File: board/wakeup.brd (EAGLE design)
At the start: 65 x 56 mm, 23 parts, among them IC2 ATMEGA48/88/168-AU, K1 PIN20X2, U1 EEPROM24

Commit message: Added gerber file
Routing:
- net GND: track 113.3 -> 104.1 mm, vias 6 -> 10
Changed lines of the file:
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@@
 <contactref element="CREE_LED1" pad="5"/>
 <contactref element="CREE_LED1" pad="7"/>
-<wire x1="28.4083875" y1="43.246209375" x2="28.4083875" y2="37.5916125" width="0.6096" layer="1"/>
-<wire x1="28.4083875" y1="37.5916125" x2="32" y2="34" width="0.6096" layer="1"/>
-<wire x1="32" y1="34" x2="32" y2="31.33" width="0.6096" layer="1"/>
 <wire x1="32" y1="31.33" x2="31.67" y2="31" width="0.6096" layer="1"/>
 <via x="37" y="36" extent="1-16" drill="0.6" shape="square"/>
@@
 <wire x1="51.44011875" y1="35.60608125" x2="51.44011875" y2="39.55988125" width="0.4064" layer="1"/>
 <wire x1="51.44011875" y1="39.55988125" x2="51" y2="40" width="0.4064" layer="1"/>
-<wire x1="61.865" y1="36.625" x2="61.865" y2="37.895" width="0" layer="19" extent="1-1"/>
-<wire x1="61.865" y1="35.355" x2="61.865" y2="36.625" width="0" layer="19" extent="1-1"/>
-<wire x1="61.865" y1="39.165" x2="61.865" y2="37.895" width="0" layer="19" extent="1-1"/>
-<wire x1="41.7074" y1="36.2" x2="42.709359375" y2="36.1917" width="0" layer="19" extent="1-1"/>
-<wire x1="20.003" y1="31" x2="22.67" y2="31" width="0" layer="19" extent="1-1"/>
-<wire x1="20.003" y1="26" x2="22.67" y2="26" width="0" layer="19" extent="1-1"/>
-<wire x1="20.003" y1="21" x2="22.67" y2="21" width="0" layer="19" extent="1-1"/>
-<wire x1="29.003" y1="16" x2="31.67" y2="16" width="0" layer="19" extent="1-1"/>
-<wire x1="22.67" y1="16" x2="22" y2="16" width="0" layer="19" extent="1-1"/>
-<wire x1="20.003" y1="16" x2="22" y2="16" width="0" layer="19" extent="1-1"/>
-<wire x1="32" y1="31.33" x2="35" y2="31" width="0" layer="19" extent="1-1"/>
-<wire x1="24" y1="42" x2="24" y2="43" width="0" layer="19" extent="1-1"/>
-<wire x1="24" y1="41" x2="24.2512625" y2="41.7487375" width="0" layer="19" extent="1-1"/>
-<wire x1="24.260740625" y1="40.260740625" x2="24" y2="41" width="0" layer="19" extent="1-1"/>
-<wire x1="24" y1="39" x2="24" y2="40" width="0" layer="19" extent="1-1"/>
-<wire x1="29.003" y1="31" x2="31.67" y2="31" width="0" layer="19" extent="1-1"/>
-<wire x1="31.67" y1="26" x2="35" y2="26" width="0" layer="19" extent="1-1"/>
-<wire x1="29.003" y1="26" x2="31.67" y2="26" width="0" layer="19" extent="1-1"/>
-<wire x1="31.67" y1="21" x2="35" y2="21" width="0" layer="19" extent="1-1"/>
-<wire x1="29.003" y1="21" x2="31.67" y2="21" width="0" layer="19" extent="1-1"/>
+<wire x1="28.4083875" y1="39" x2="28.4083875" y2="43.246209375" width="0.4064" layer="1"/>
+<via x="30.1" y="44" extent="1-16" drill="0.9" shape="square"/>
+<via x="30.1" y="42" extent="1-16" drill="0.9" shape="square"/>
+<via x="30.1" y="40" extent="1-16" drill="0.9" shape="square"/>
+<via x="30.1" y="38" extent="1-16" drill="0.9" shape="square"/>
+<polygon width="0.4064" layer="1">
+<vertex x="28" y="37"/>
+<vertex x="28" y="45"/>
+<vertex x="31" y="45"/>
+<vertex x="31" y="37"/>
+</polygon>
 </signal>
 <signal name="+3V3">
@@
 <signal name="N$1">
 </signal>
+<signal name="N$2">
+</signal>
 </signals>

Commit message: Added pin header for tm1637 7-Segment display
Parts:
- added SL3: (no value), con-amp-quick:04P
- moved SL2 7.07 mm to (45.0, 43.0)
- moved C2 1.41 mm to (39.0, 35.0), turned to 90 degrees
- moved C3 1.41 mm to (39.0, 39.0), turned to 270 degrees
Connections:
- net +5V: now also SL3.1
- net GND: now also SL3.4
- net MISO_SPI: now also SL3.2
- net SCLK_SPI: now also SL3.3
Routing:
- net +5V: track 44.0 -> 73.5 mm
- net SCLK_SPI: track 0.00 -> 9.04 mm
- net MISO_SPI: track 0.00 -> 9.04 mm
- net VCC: track 65.2 -> 59.5 mm
- net GND: track 104.1 -> 101.5 mm
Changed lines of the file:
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@@
 <attribute name="OC_NEWARK" value="unknown" x="12" y="28" size="1.778" layer="27" rot="R90" display="off"/>
 </element>
-<element name="SL2" library="con-amp-quick" package="02P" value="" x="38" y="44" rot="R180">
-<attribute name="MF" value="" x="38" y="44" size="1.778" layer="27" rot="R180" display="off"/>
-<attribute name="MPN" value="" x="38" y="44" size="1.778" layer="27" rot="R180" display="off"/>
-<attribute name="OC_FARNELL" value="unknown" x="38" y="44" size="1.778" layer="27" rot="R180" display="off"/>
-<attribute name="OC_NEWARK" value="unknown" x="38" y="44" size="1.778" layer="27" rot="R180" display="off"/>
+<element name="SL2" library="con-amp-quick" package="02P" value="" x="45" y="43" rot="R180">
+<attribute name="MF" value="" x="45" y="43" size="1.778" layer="27" rot="R180" display="off"/>
+<attribute name="MPN" value="" x="45" y="43" size="1.778" layer="27" rot="R180" display="off"/>
+<attribute name="OC_FARNELL" value="unknown" x="45" y="43" size="1.778" layer="27" rot="R180" display="off"/>
+<attribute name="OC_NEWARK" value="unknown" x="45" y="43" size="1.778" layer="27" rot="R180" display="off"/>
 </element>
-<element name="C2" library="rcl" package="C0805" value="47nF" x="38" y="34" rot="R180"/>
+<element name="C2" library="rcl" package="C0805" value="47nF" x="39" y="35" rot="R90"/>
 <element name="U$7" library="1" package="SOT" value="AMC7135" x="32" y="31" rot="R270"/>
 <element name="U$8" library="1" package="SOT" value="AMC7135" x="23" y="31" rot="R270"/>
@@
 <element name="U$6" library="1" package="SOT" value="AMC7135" x="32" y="16" rot="R270"/>
 <element name="IC2" library="atmega8" package="TQFP32-08" value="ATMEGA48/88/168-AU" x="46" y="35"/>
-<element name="C3" library="rcl" package="C0805" value="47nF" x="38" y="38" rot="R180"/>
+<element name="C3" library="rcl" package="C0805" value="47nF" x="39" y="39" rot="R270"/>
 <element name="J1" library="con-jack" package="SPC4078" value="" x="12" y="13" rot="R90">
 <attribute name="OC_FARNELL" value="unknown" x="12" y="13" size="1.778" layer="27" rot="R90" display="off"/>
@@
 </element>
 <element name="CREE_LED1" library="CreeXL-MC-E" package="CREE_XL_MCE" value="CREE_XL_MCE" x="24" y="41" rot="R90"/>
+<element name="SL3" library="con-amp-quick" package="04P" value="" x="37" y="43">
+<attribute name="MF" value="" x="37" y="43" size="1.778" layer="27" display="off"/>
+<attribute name="OC_NEWARK" value="unknown" x="37" y="43" size="1.778" layer="27" display="off"/>
+<attribute name="OC_FARNELL" value="unknown" x="37" y="43" size="1.778" layer="27" display="off"/>
+<attribute name="MPN" value="" x="37" y="43" size="1.778" layer="27" display="off"/>
+</element>
 </elements>
 <signals>
@@
 <wire x1="62" y1="30" x2="62" y2="32.4225" width="0.4064" layer="1"/>
 <wire x1="62" y1="32.4225" x2="62.075" y2="32.4975" width="0.4064" layer="1"/>
-<wire x1="37.05" y1="38" x2="36.73" y2="38.32" width="0.4064" layer="1"/>
-<wire x1="36.73" y1="38.32" x2="36.73" y2="44" width="0.4064" layer="1"/>
 <contactref element="J1" pad="2"/>
 <contactref element="J1" pad="1"/>
 <wire x1="29.003" y1="16" x2="22" y2="16" width="0.6096" layer="1"/>
-<wire x1="41.7074" y1="34.6" x2="42.6" y2="34.6" width="0.4064" layer="1"/>
-<wire x1="42.6" y1="34.6" x2="43" y2="35" width="0.4064" layer="1"/>
-<wire x1="43" y1="35" x2="43" y2="35.901059375" width="0.4064" layer="1"/>
-<wire x1="43" y1="35.901059375" x2="42.709359375" y2="36.1917" width="0.4064" layer="1"/>
 <contactref element="CREE_LED1" pad="8"/>
 <contactref element="CREE_LED1" pad="6"/>
@@
 <contactref element="CREE_LED1" pad="7"/>
 <wire x1="32" y1="31.33" x2="31.67" y2="31" width="0.6096" layer="1"/>
-<via x="37" y="36" extent="1-16" drill="0.6" shape="square"/>
-<wire x1="37.05" y1="34" x2="37.05" y2="38" width="0.4064" layer="1"/>
-<wire x1="42.709359375" y1="36.1917" x2="37.1917" y2="36.1917" width="0.4064" layer="1"/>
-<wire x1="37.1917" y1="36.1917" x2="37" y2="36" width="0.4064" layer="1" curve="90"/>
+<via x="37" y="37" extent="1-16" drill="0.6" shape="square"/>
 <via x="35" y="31" extent="1-16" drill="0.9" shape="square"/>
 <via x="35" y="26" extent="1-16" drill="0.9" shape="square"/>
@@
 <vertex x="31" y="37"/>
 </polygon>
+<contactref element="SL3" pad="4"/>
+<wire x1="39" y1="35.95" x2="38.05" y2="35.95" width="0.4064" layer="1"/>
+<wire x1="38.05" y1="35.95" x2="37" y2="37" width="0.4064" layer="1"/>
+<wire x1="39" y1="38.05" x2="38.05" y2="38.05" width="0.4064" layer="1"/>
+<wire x1="38.05" y1="38.05" x2="37" y2="37" width="0.4064" layer="1"/>
+<wire x1="43.20988125" y1="37.79011875" x2="42" y2="39" width="0.4064" layer="1"/>
+<wire x1="42" y1="39" x2="41" y2="39" width="0.4064" layer="1"/>
+<wire x1="41" y1="39" x2="40" y2="38" width="0.4064" layer="1"/>
+<wire x1="40" y1="38" x2="39" y2="38" width="0.4064" layer="1"/>
+<wire x1="43.20988125" y1="37.79011875" x2="43.20988125" y2="36" width="0.4064" layer="1"/>
+<wire x1="43.20988125" y1="36" x2="43.20988125" y2="34.8705625" width="0.4064" layer="1"/>
+<wire x1="43.20988125" y1="34.8705625" x2="42.93931875" y2="34.6" width="0.4064" layer="1"/>
+<wire x1="42.93931875" y1="34.6" x2="41.7074" y2="34.6" width="0.4064" layer="1"/>
+<wire x1="41.7074" y1="36.2" x2="43.00988125" y2="36.2" width="0.4064" layer="1"/>
+<wire x1="43.00988125" y1="36.2" x2="43.20988125" y2="36" width="0.4064" layer="1" curve="-90"/>
 </signal>
 <signal name="+3V3">
@@
 <wire x1="8.37" y1="53.77" x2="7" y2="52.4" width="0.6096" layer="1"/>
 <wire x1="10.91" y1="53.77" x2="8.37" y2="53.77" width="0.6096" layer="1"/>
-<wire x1="7" y1="30" x2="7" y2="52.4" width="0.6096" layer="1"/>
 <contactref element="J1" pad="3"/>
 <wire x1="12" y1="26.73" x2="12" y2="16" width="0.6096" layer="1"/>
 <wire x1="7" y1="30" x2="10.27" y2="26.73" width="0.6096" layer="1"/>
 <wire x1="10.27" y1="26.73" x2="12" y2="26.73" width="0.6096" layer="1"/>
+<contactref element="SL3" pad="1"/>
+<wire x1="33.19" y1="43" x2="33.19" y2="45.81" width="0.6096" layer="1"/>
+<wire x1="33.19" y1="45.81" x2="32" y2="47" width="0.6096" layer="1"/>
+<wire x1="32" y1="47" x2="7" y2="47" width="0.6096" layer="1"/>
+<wire x1="7" y1="30" x2="7" y2="47" width="0.6096" layer="1"/>
+<wire x1="7" y1="47" x2="7" y2="52.4" width="0.6096" layer="1"/>
 <wire x1="12" y1="21.65" x2="12" y2="24.19" width="0" layer="19" extent="1-1"/>
 <wire x1="12" y1="19.11" x2="12" y2="21.65" width="0" layer="19" extent="1-1"/>
@@
 <contactref element="C3" pad="1"/>
 <wire x1="41.7074" y1="33.8" x2="39.15" y2="33.8" width="0.4064" layer="1"/>
-<wire x1="39.15" y1="33.8" x2="38.95" y2="34" width="0.4064" layer="1"/>
-<wire x1="41.7074" y1="35.4" x2="40.35" y2="35.4" width="0.4064" layer="1"/>
-<wire x1="40.35" y1="35.4" x2="38.95" y2="34" width="0.4064" layer="1"/>
-<wire x1="38.95" y1="38" x2="39.27" y2="38.32" width="0.4064" layer="1"/>
-<wire x1="39.27" y1="38.32" x2="39.27" y2="44" width="0.4064" layer="1"/>
-<wire x1="38.95" y1="38" x2="39" y2="37.95" width="0.4064" layer="1"/>
-<wire x1="39" y1="37.95" x2="40.05" y2="39" width="0.4064" layer="1"/>
-<wire x1="40.05" y1="39" x2="42" y2="39" width="0.4064" layer="1"/>
-<wire x1="42" y1="39" x2="44" y2="37" width="0.4064" layer="1"/>
-<wire x1="44" y1="37" x2="44" y2="35" width="0.4064" layer="1"/>
-<wire x1="44" y1="35" x2="42.8" y2="33.8" width="0.4064" layer="1"/>
-<wire x1="42.8" y1="33.8" x2="41.7074" y2="33.8" width="0.4064" layer="1"/>
 <wire x1="52.106340625" y1="31.893659375" x2="52.106340625" y2="40.893659375" width="0.4064" layer="1"/>
-<wire x1="52.106340625" y1="40.893659375" x2="49" y2="44" width="0.4064" layer="1"/>
-<wire x1="49" y1="44" x2="39.27" y2="44" width="0.4064" layer="1"/>
 <wire x1="52.106340625" y1="31.893659375" x2="59" y2="25" width="0.4064" layer="1"/>
 <wire x1="59" y1="25" x2="59" y2="18.19" width="0.4064" layer="1"/>
 <wire x1="59" y1="18.19" x2="57.54" y2="16.73" width="0.4064" layer="1"/>
+<wire x1="52.106340625" y1="40.893659375" x2="50" y2="43" width="0.4064" layer="1"/>
+<wire x1="50" y1="43" x2="46.27" y2="43" width="0.4064" layer="1"/>
+<wire x1="39" y1="39.95" x2="40.95" y2="39.95" width="0.4064" layer="1"/>
+<wire x1="40.95" y1="39.95" x2="42" y2="41" width="0.4064" layer="1"/>
+<wire x1="42" y1="41" x2="44.27" y2="41" width="0.4064" layer="1"/>
+<wire x1="44.27" y1="41" x2="46.27" y2="43" width="0.4064" layer="1"/>
+<wire x1="39" y1="39.95" x2="36.95" y2="39.95" width="0.4064" layer="1"/>
+<wire x1="36.95" y1="39.95" x2="36" y2="39" width="0.4064" layer="1"/>
+<wire x1="36" y1="39" x2="36" y2="35" width="0.4064" layer="1"/>
+<wire x1="36" y1="35" x2="36.95" y2="34.05" width="0.4064" layer="1"/>
+<wire x1="36.95" y1="34.05" x2="39" y2="34.05" width="0.4064" layer="1"/>
+<wire x1="41.7074" y1="35.4" x2="40.723959375" y2="35.4" width="0.4064" layer="1"/>
+<wire x1="40.723959375" y1="35.4" x2="39.373959375" y2="34.05" width="0.4064" layer="1"/>
+<wire x1="39.373959375" y1="34.05" x2="39" y2="34.05" width="0.4064" layer="1"/>
+<wire x1="39" y1="34.05" x2="39.15" y2="33.8" width="0" layer="19" extent="1-1"/>
 </signal>
 <signal name="MOSI">
@@
 <signal name="MISO_SPI">
 <contactref element="K1" pad="21"/>
+<contactref element="SL3" pad="2"/>
+<wire x1="35.73" y1="43" x2="35.73" y2="49.27" width="0.4064" layer="1"/>
+<wire x1="35.73" y1="49.27" x2="33.77" y2="51.23" width="0.4064" layer="1"/>
 </signal>
 <signal name="SCLK_SPI">
 <contactref element="K1" pad="23"/>
+<contactref element="SL3" pad="3"/>
+<wire x1="38.27" y1="43" x2="38.27" y2="49.27" width="0.4064" layer="1"/>
+<wire x1="38.27" y1="49.27" x2="36.31" y2="51.23" width="0.4064" layer="1"/>
 </signal>
 <signal name="N$1">

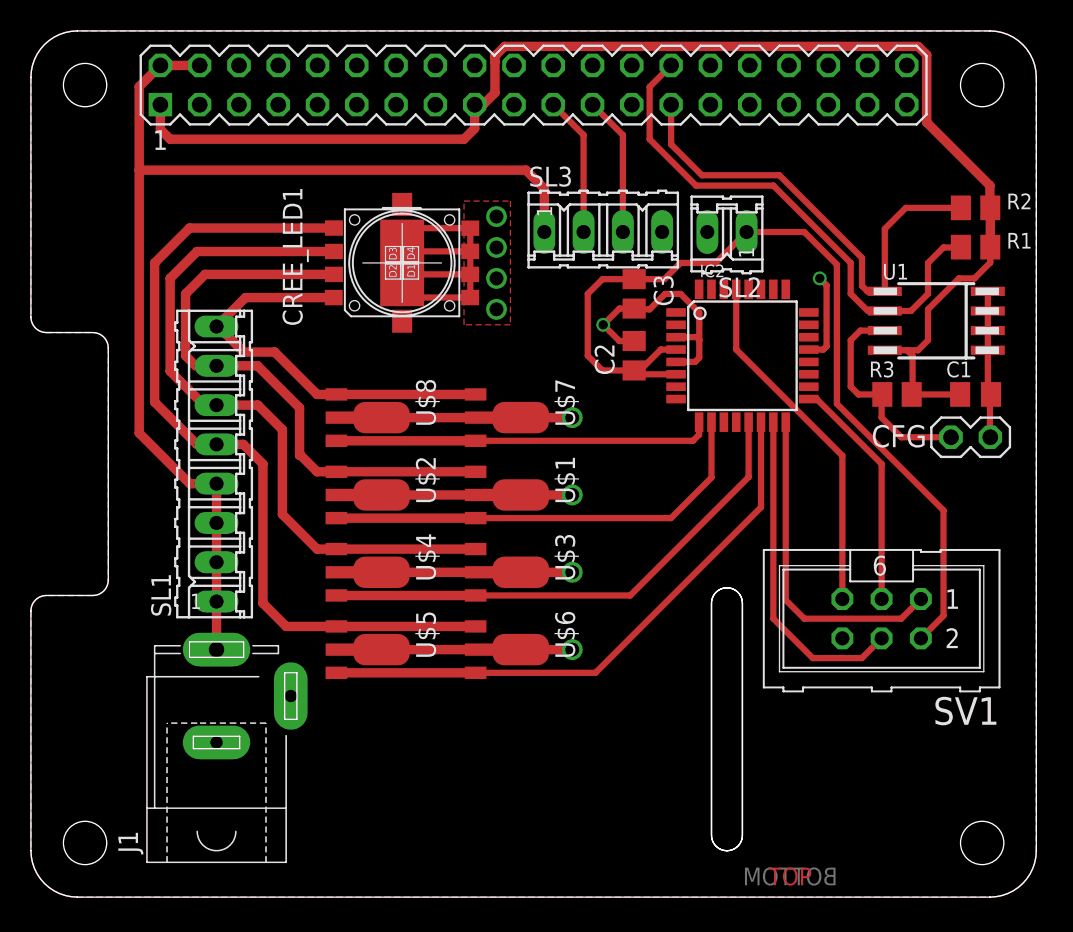
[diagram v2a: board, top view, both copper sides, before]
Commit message: Fixed FCC net, added I2C nets
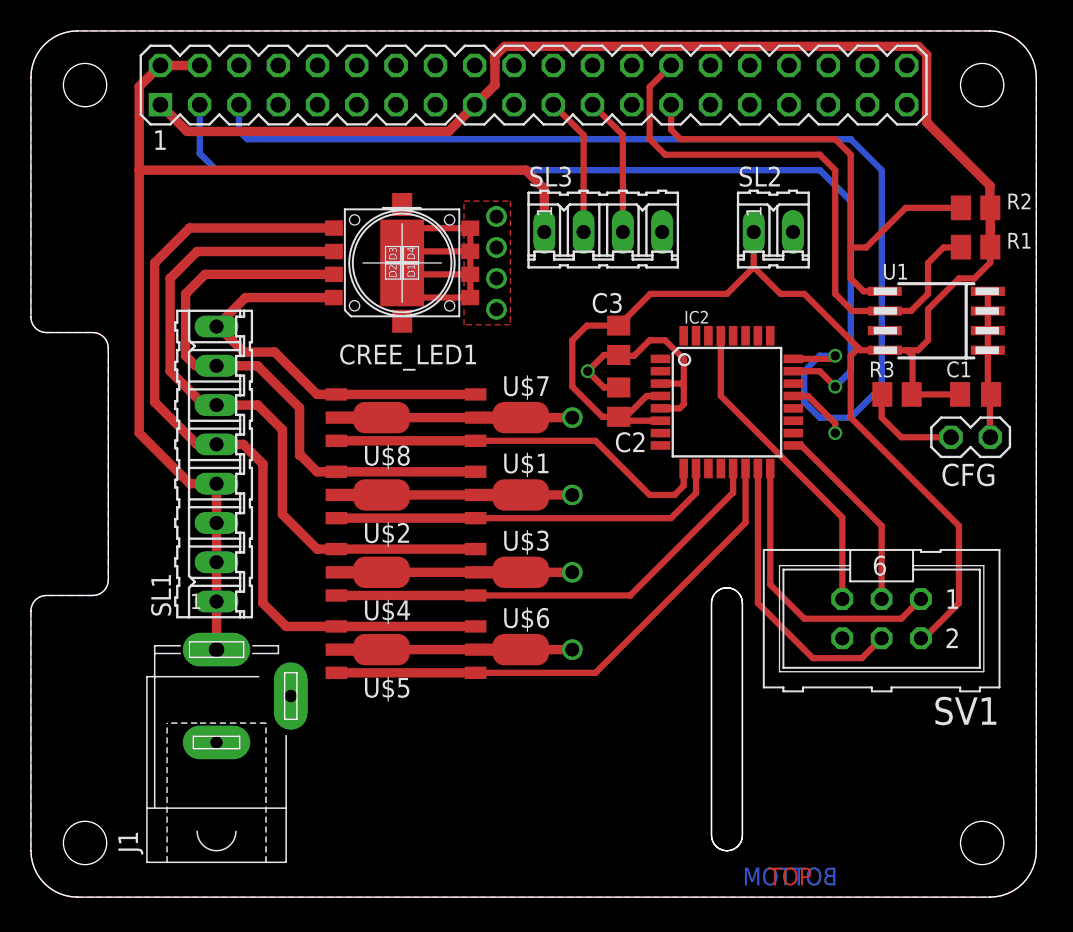
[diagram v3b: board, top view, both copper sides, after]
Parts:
- moved C2 3.16 mm to (38.0, 32.0)
- moved C3 3.16 mm to (38.0, 36.0)
- moved IC2 3.16 mm to (45.0, 32.0)
- moved SL2 3.00 mm to (48.0, 43.0), turned to 0 degrees
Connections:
- removed net VCC: C2.1, C3.1, IC2.4, IC2.6, SL2.1, SV1.2
- net +3V3: now also C2.1, C3.1, IC2.4, IC2.6, SL2.1, SV1.2
- net I2C_SCL1: now also IC2.24
- net I2C_SDA1: now also IC2.23
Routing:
- net I2C_SCL1: track 0.00 -> 71.7 mm, vias 0 -> 1
- net I2C_SDA1: track 0.00 -> 62.0 mm, vias 0 -> 1
- net +3V3: track 88.0 -> 148.2 mm
- net VCC: track 59.5 -> 0.00 mm
- net N$3: track 14.2 -> 6.53 mm
- net SCL0_I2C_ID_EEPROM: track 33.0 -> 37.6 mm
- net WHITE_LED: track 37.4 -> 34.0 mm
- net GREEN_LED: track 28.9 -> 25.5 mm
- net BLUE_LED: track 33.4 -> 30.0 mm
- net SCK: track 15.2 -> 12.6 mm
- net RESET: track 22.9 -> 20.3 mm
- net MOSI: track 21.3 -> 18.7 mm
- net MISO: track 21.3 -> 18.7 mm
- net SDA0_I2C_ID_EEPROM: track 30.9 -> 32.6 mm
- net GND: track 101.5 -> 100.5 mm
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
